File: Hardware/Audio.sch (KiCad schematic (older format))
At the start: 0 parts

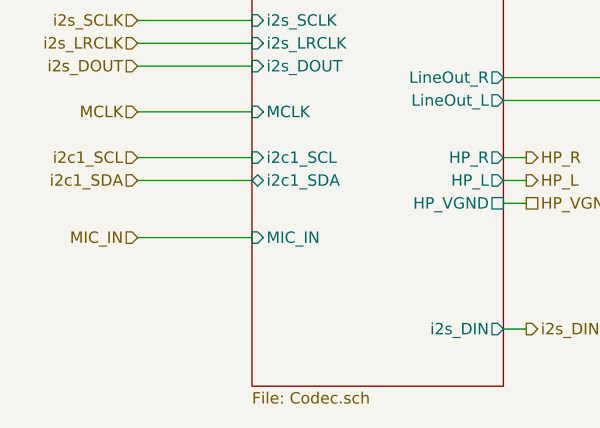
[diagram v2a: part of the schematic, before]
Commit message: Changing around the audio inputs.
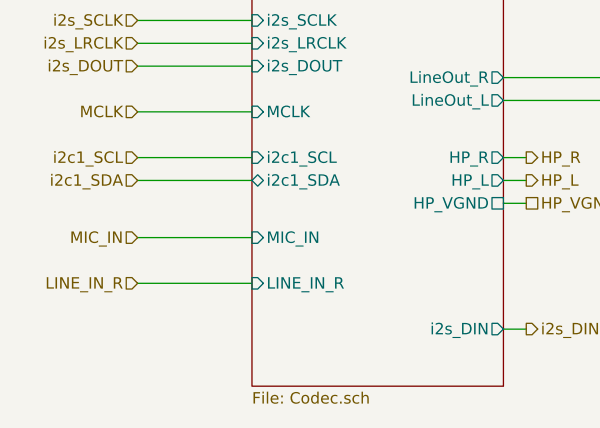
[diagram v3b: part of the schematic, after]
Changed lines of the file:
@@
 F13 "HP_L" O R 5550 3400 50
 F14 "HP_VGND" U R 5550 3500 50
+F15 "LINE_IN_R" I L 4450 3850 50
 $EndSheet
 $Sheet
@@
 Wire Wire Line
 	7200 3700 7300 3700
+Text HLabel 3950 3850 0    50   Input ~ 0
+LINE_IN_R
+Wire Wire Line
+	3950 3850 4450 3850
 $EndSCHEMATC
